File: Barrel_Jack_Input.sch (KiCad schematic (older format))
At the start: 12 parts, among them J3 Barrel_Jack_MountingPin, Q23 VBA2625, Q24 VBA2625, Q25 2n7002K, Q26 VBA2625, Q27 VBA2625

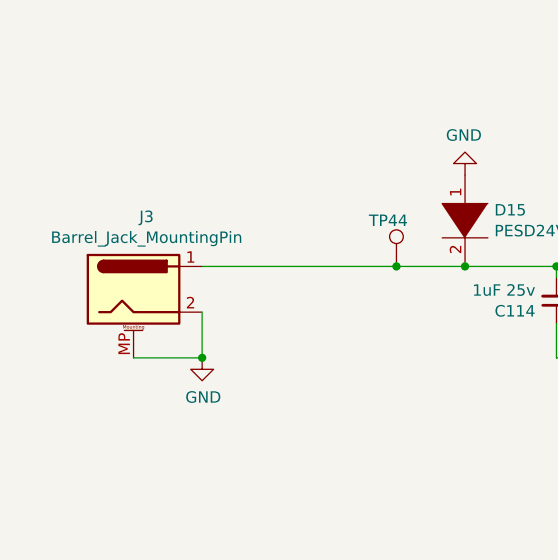
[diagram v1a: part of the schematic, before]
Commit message: Layout placed type-c + barrel jack
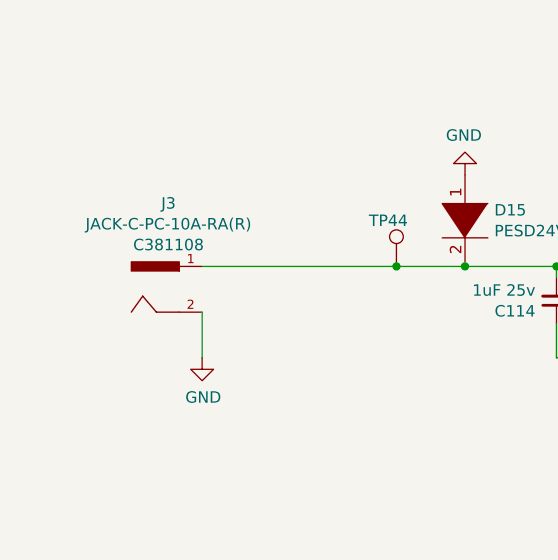
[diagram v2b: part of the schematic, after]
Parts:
- removed J3: Barrel_Jack_MountingPin, Connector_BarrelJack:BarrelJack_Horizontal, symbol Connector:Barrel_Jack_MountingPin
- added J3: JACK-C-PC-10A-RA(R), GLOBTECK_JACK-C-PC-10A-RA(R), symbol SmartBattery:JACK-C-PC-10A-RA(R)
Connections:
- net BARREL_RAW: now also J3.1
- net GND: now also J3.2
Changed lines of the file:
@@
 $Descr A4 11693 8268
 encoding utf-8
-Sheet 9 10
+Sheet 7 10
 Title ""
 Date ""
@@
 Comment4 ""
 $EndDescr
-$Comp
-L Connector:Barrel_Jack_MountingPin J?
-U 1 1 5FF4E84B
-P 3100 3150
-AR Path="/5FF4E84B" Ref="J?"  Part="1"
-AR Path="/5FF4A13F/5FF4E84B" Ref="J3"  Part="1"
-F 0 "J3" H 3157 3467 50  0000 C CNN
-F 1 "Barrel_Jack_MountingPin" H 3157 3376 50  0000 C CNN
-F 2 "Connector_BarrelJack:BarrelJack_Horizontal" H 3150 3110 50  0001 C CNN
-F 3 "~" H 3150 3110 50  0001 C CNN
-F 4 "320120003" H 3100 3150 50  0001 C CNN "SKU"
-	1    3100 3150
-	1    0    0    -1
-$EndComp
-Wire Wire Line
-	3100 3450 3400 3450
 $Comp
 L SmartBattery:VBA2625 Q?
@@
 Wire Wire Line
 	3400 3250 3400 3450
-Connection ~ 3400 3450
 $Comp
 L power:GND #PWR0200
@@
 Text HLabel 5700 3600 2    50   Input ~ 0
 BARREL_RAW
+$Comp
+L SmartBattery:JACK-C-PC-10A-RA(R) J3
+U 1 1 6008EB42
+P 3200 3150
+F 0 "J3" H 3147 3526 50  0000 C CNN
+F 1 "JACK-C-PC-10A-RA(R)" H 3147 3435 50  0000 C CNN
+F 2 "GLOBTECK_JACK-C-PC-10A-RA(R)" H 3200 3150 50  0001 L BNN
+F 3 "" H 3200 3150 50  0001 L BNN
+F 4 "Manufacturer Recommendations" H 3200 3150 50  0001 L BNN "STANDARD"
+F 5 "Globe Tek" H 3200 3150 50  0001 L BNN "MANUFACTURER"
+F 6 "A" H 3200 3150 50  0001 L BNN "PARTREV"
+F 7 "C381108" H 3147 3344 50  0000 C CNN "LCSC"
+	1    3200 3150
+	-1   0    0    -1
+$EndComp
 $EndSCHEMATC

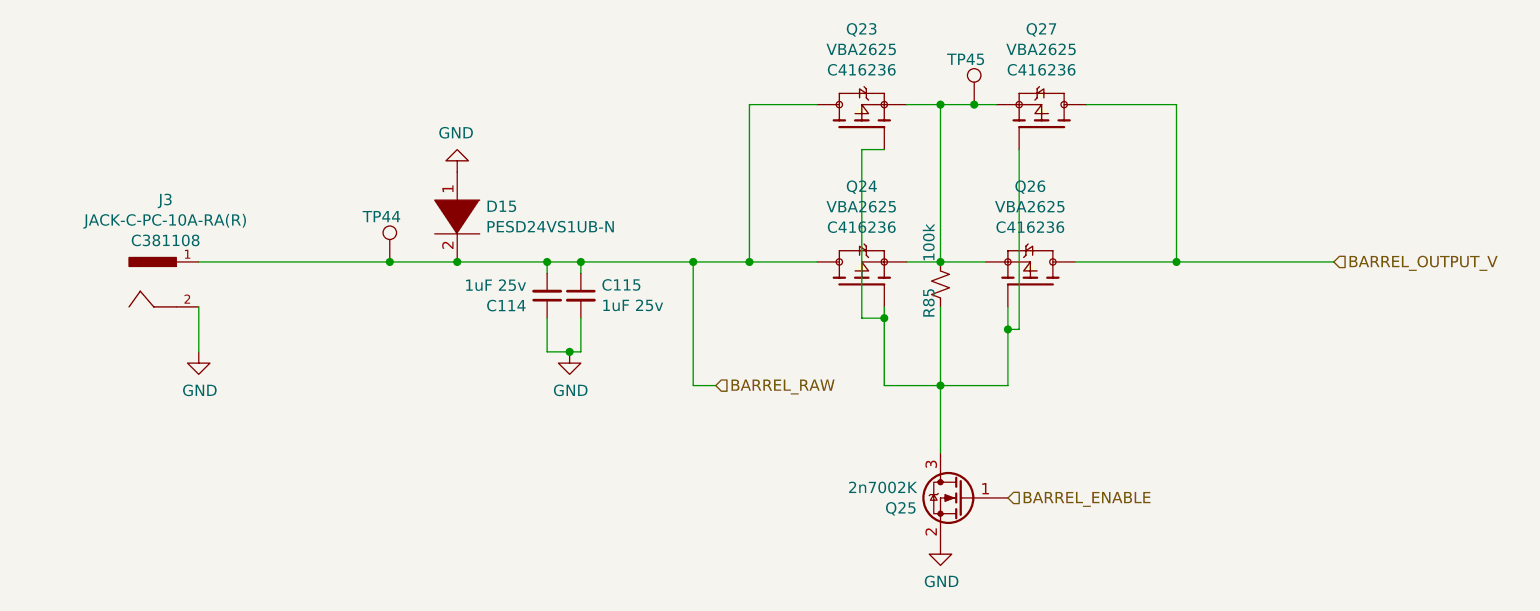
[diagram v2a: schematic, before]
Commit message: lots of GPIO connectivity changes. fixed no PD on input fixed CH340G leakage. can otherwise power from GPIO. added fet for powering VCONN from 3v/5v NEED TO ADD OVERCURRENT
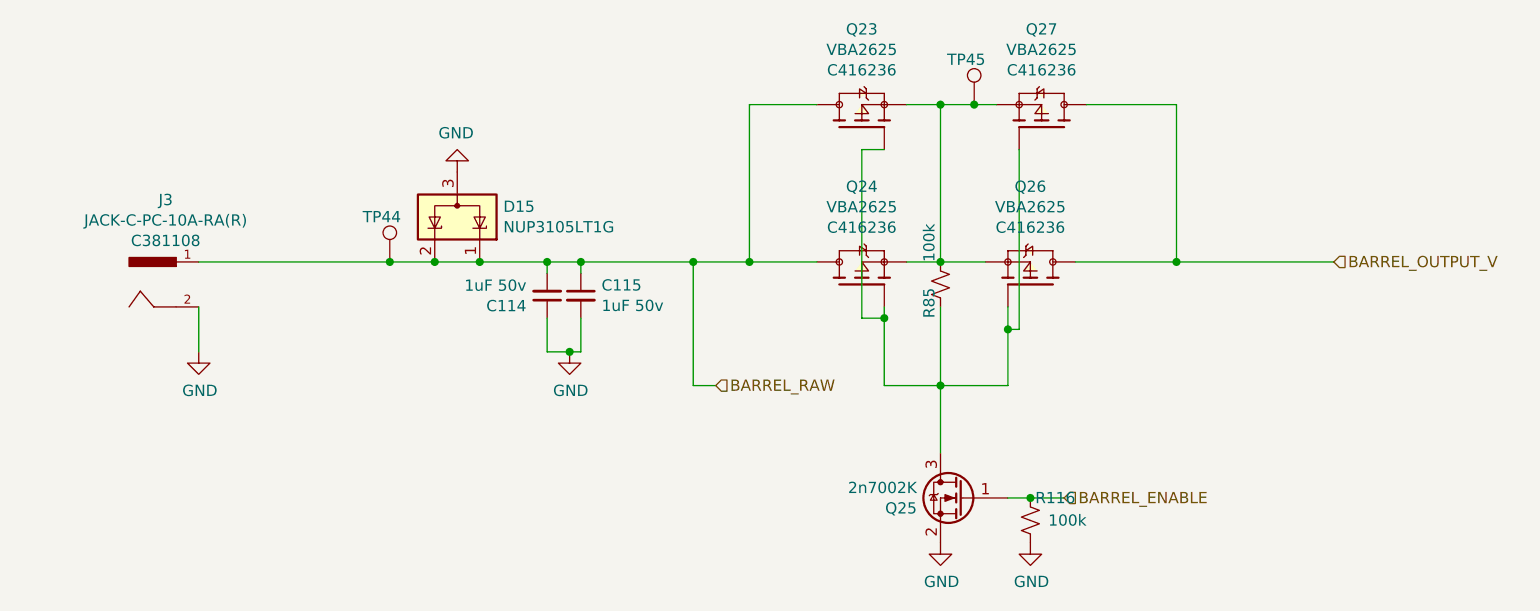
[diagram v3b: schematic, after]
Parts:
- removed D15: PESD24VS1UB-N, lc_lib:SOD-523, symbol pspice:DIODE
- added D15: NUP3105LT1G, Package_TO_SOT_SMD:SOT-23, symbol Power_Protection:SP0502BAJT
- added R116: 100k, lc_lib:0402_R, symbol Device:R_Small_US
- C114, C115: value 1uF 25v -> 1uF 50v
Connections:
- net BARREL_ENABLE: now also R116.2
- net BARREL_RAW: now also D15.1 (K), D15.2 (K)
- net GND: now also D15.3 (A), R116.1
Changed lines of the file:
@@
 AR Path="/5FF4A13F/5FF697F8" Ref="C115"  Part="1"
 F 0 "C115" H 5192 3246 50  0000 L CNN
-F 1 "1uF 25v" H 5192 3155 50  0000 L CNN
+F 1 "1uF 50v" H 5192 3155 50  0000 L CNN
 F 2 "lc_lib:0402_C" H 5100 3200 50  0001 C CNN
 F 3 "~" H 5100 3200 50  0001 C CNN
@@
 AR Path="/5FF4A13F/5FF69802" Ref="C114"  Part="1"
 F 0 "C114" H 5042 3246 50  0000 L CNN
-F 1 "1uF 25v" H 5042 3155 50  0000 L CNN
+F 1 "1uF 50v" H 5042 3155 50  0000 L CNN
 F 2 "lc_lib:0402_C" H 4950 3200 50  0001 C CNN
 F 3 "~" H 4950 3200 50  0001 C CNN
@@
 $EndComp
 Wire Wire Line
-	4250 3050 4550 3050
-Wire Wire Line
 	4950 3050 4950 3100
 Connection ~ 4950 3050
 Wire Wire Line
 	4950 3050 5100 3050
-$Comp
-L pspice:DIODE D?
-U 1 1 5FF6980D
-P 4550 2850
-AR Path="/5FF971C1/5FF6980D" Ref="D?"  Part="1"
-AR Path="/5FF4A13F/5FF6980D" Ref="D15"  Part="1"
-F 0 "D15" V 4504 2978 50  0000 L CNN
-F 1 "PESD24VS1UB-N" V 4595 2978 50  0000 L CNN
-F 2 "lc_lib:SOD-523" H 4550 2850 50  0001 C CNN
-F 3 "~" H 4550 2850 50  0001 C CNN
-F 4 "C316036" V 4550 2850 50  0001 C CNN "lcsc"
-	1    4550 2850
-	0    1    1    0
-$EndComp
-Connection ~ 4550 3050
-Wire Wire Line
-	4550 3050 4950 3050
 $Comp
 L power:GND #PWR?
@@
 Text HLabel 8450 3050 2    50   Input ~ 0
 BARREL_OUTPUT_V
-Text HLabel 7000 4100 2    50   Input ~ 0
+Text HLabel 7250 4100 2    50   Input ~ 0
 BARREL_ENABLE
 Wire Wire Line
@@
 	-1   0    0    -1
 $EndComp
+Wire Wire Line
+	7250 4100 7100 4100
+$Comp
+L Power_Protection:SP0502BAJT D?
+U 1 1 602F31F8
+P 4550 2850
+AR Path="/600C8F88/602F31F8" Ref="D?"  Part="1"
+AR Path="/5FF4A13F/602F31F8" Ref="D15"  Part="1"
+F 0 "D15" H 4345 2804 50  0000 R CNN
+F 1 "NUP3105LT1G" H 4345 2895 50  0000 R CNN
+F 2 "Package_TO_SOT_SMD:SOT-23" H 4775 2800 50  0001 L CNN
+F 3 "http://www.littelfuse.com/~/media/files/littelfuse/technical%20resources/documents/data%20sheets/sp05xxba.pdf" H 4675 2975 50  0001 C CNN
+F 4 "C133092" H 4550 2850 50  0001 C CNN "LCSC"
+	1    4550 2850
+	-1   0    0    1
+$EndComp
+Wire Wire Line
+	4250 3050 4450 3050
+Wire Wire Line
+	4650 3050 4950 3050
+Wire Wire Line
+	4450 3050 4650 3050
+Connection ~ 4450 3050
+Connection ~ 4650 3050
+$Comp
+L Device:R_Small_US R?
+U 1 1 602FB01A
+P 7100 4200
+AR Path="/5FD99B08/602FB01A" Ref="R?"  Part="1"
+AR Path="/5FF1D194/602FB01A" Ref="R?"  Part="1"
+AR Path="/5FF971C1/602FB01A" Ref="R?"  Part="1"
+AR Path="/602FB01A" Ref="R?"  Part="1"
+AR Path="/5FF4A13F/602FB01A" Ref="R116"  Part="1"
+F 0 "R116" H 6900 4100 50  0000 L CNN
+F 1 "100k" H 6850 4200 50  0000 L CNN
+F 2 "lc_lib:0402_R" H 7100 4200 50  0001 C CNN
+F 3 "~" H 7100 4200 50  0001 C CNN
+F 4 "C25741" V 7100 4200 50  0001 C CNN "LCSC"
+	1    7100 4200
+	-1   0    0    1
+$EndComp
+$Comp
+L power:GND #PWR0256
+U 1 1 602FB7DC
+P 7100 4300
+F 0 "#PWR0256" H 7100 4050 50  0001 C CNN
+F 1 "GND" H 7105 4127 50  0000 C CNN
+F 2 "" H 7100 4300 50  0001 C CNN
+F 3 "" H 7100 4300 50  0001 C CNN
+	1    7100 4300
+	1    0    0    -1
+$EndComp
+Connection ~ 7100 4100
+Wire Wire Line
+	7100 4100 7000 4100
 $EndSCHEMATC
